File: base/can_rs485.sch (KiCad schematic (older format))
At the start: 15 parts, among them U21 SN65HVD230

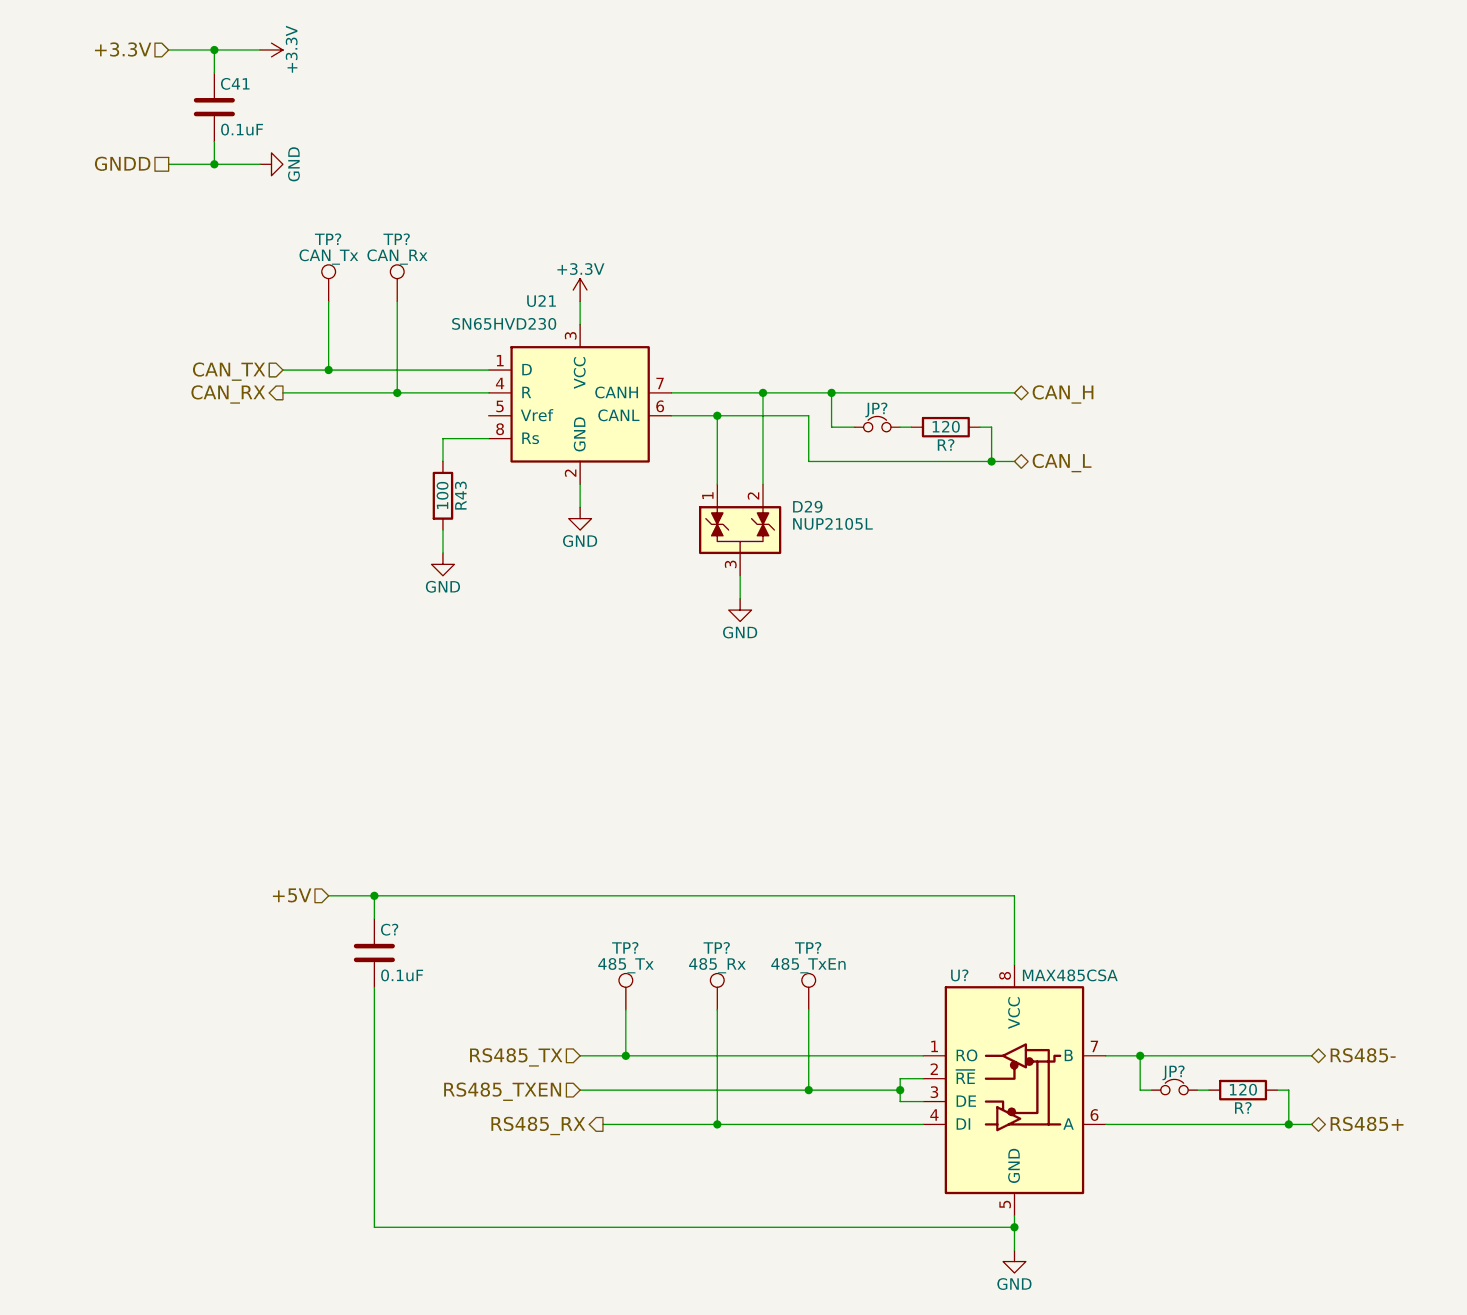
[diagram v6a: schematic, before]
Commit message: annotate sch
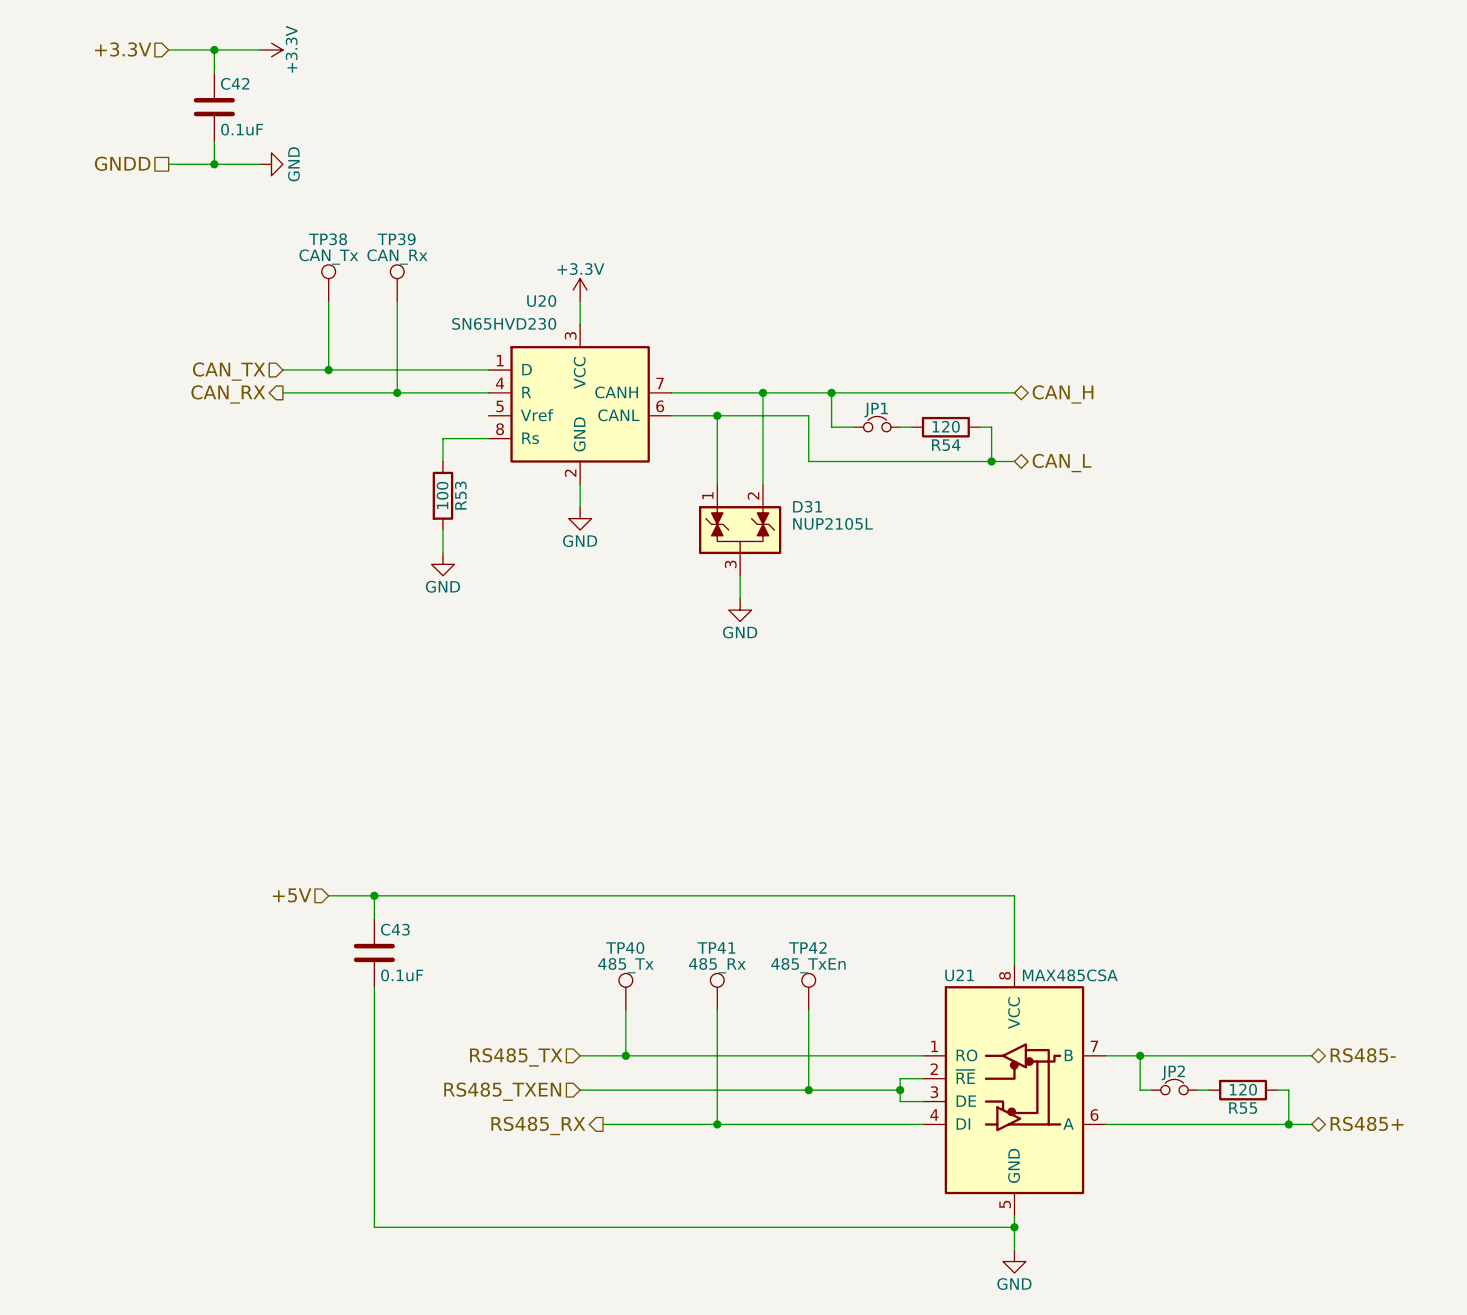
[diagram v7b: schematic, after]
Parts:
- gave numbers to parts that had none: 11
- renumbered C41 to C42, D29 to D31, R43 to R53, U21 to U20
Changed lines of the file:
@@
 +5V
 $Comp
-L SN65HVD230 U21
+L SN65HVD230 U20
 U 1 1 5A3C3395
 P 3100 2400
-F 0 "U21" H 3000 2800 50  0000 R CNN
+F 0 "U20" H 3000 2800 50  0000 R CNN
 F 1 "SN65HVD230" H 3000 2700 50  0000 R CNN
 F 2 "Package_SOIC:SOIC-8_3.9x4.9mm_P1.27mm" H 3100 1900 50  0001 C CNN
@@
 	3500 2400 5000 2400
 $Comp
-L C C41
+L C C42
 U 1 1 5A3C342C
 P 1500 1150
-F 0 "C41" H 1525 1250 50  0000 L CNN
+F 0 "C42" H 1525 1250 50  0000 L CNN
 F 1 "0.1uF" H 1525 1050 50  0000 L CNN
 F 2 "Capacitor_SMD:C_0603_1608Metric" H 1538 1000 50  0001 C CNN
@@
 GNDD
 $Comp
-L +3.3V #PWR027
+L +3.3V #PWR33
 U 1 1 5A3C351C
 P 1700 900
-F 0 "#PWR027" H 1700 750 50  0001 C CNN
+F 0 "#PWR33" H 1700 750 50  0001 C CNN
 F 1 "+3.3V" H 1700 1040 50  0000 C CNN
 F 2 "" H 1700 900 50  0001 C CNN
@@
 $EndComp
 $Comp
-L GND #PWR028
+L GND #PWR34
 U 1 1 5A3C3534
 P 1700 1400
-F 0 "#PWR028" H 1700 1150 50  0001 C CNN
+F 0 "#PWR34" H 1700 1150 50  0001 C CNN
 F 1 "GND" H 1700 1250 50  0000 C CNN
 F 2 "" H 1700 1400 50  0001 C CNN
@@
 $EndComp
 $Comp
-L GND #PWR029
+L GND #PWR37
 U 1 1 5A3C354C
 P 3100 2900
-F 0 "#PWR029" H 3100 2650 50  0001 C CNN
+F 0 "#PWR37" H 3100 2650 50  0001 C CNN
 F 1 "GND" H 3100 2750 50  0000 C CNN
 F 2 "" H 3100 2900 50  0001 C CNN
@@
 	3100 2900 3100 2800
 $Comp
-L +3.3V #PWR030
+L +3.3V #PWR36
 U 1 1 5A3C3569
 P 3100 2000
-F 0 "#PWR030" H 3100 1850 50  0001 C CNN
+F 0 "#PWR36" H 3100 1850 50  0001 C CNN
 F 1 "+3.3V" H 3100 2140 50  0000 C CNN
 F 2 "" H 3100 2000 50  0001 C CNN
@@
 	3100 2100 3100 2000
 $Comp
-L R R43
+L R R53
 U 1 1 5A3C3843
 P 2500 2850
-F 0 "R43" V 2580 2850 50  0000 C CNN
+F 0 "R53" V 2580 2850 50  0000 C CNN
 F 1 "100" V 2500 2850 50  0000 C CNN
 F 2 "Resistor_SMD:R_0603_1608Metric" V 2430 2850 50  0001 C CNN
@@
 	2500 3000 2500 3100
 $Comp
-L GND #PWR031
+L GND #PWR35
 U 1 1 5A3C38B7
 P 2500 3100
-F 0 "#PWR031" H 2500 2850 50  0001 C CNN
+F 0 "#PWR35" H 2500 2850 50  0001 C CNN
 F 1 "GND" H 2500 2950 50  0000 C CNN
 F 2 "" H 2500 3100 50  0001 C CNN
@@
 	1800 2400 2700 2400
 $Comp
-L NUP2105L D29
+L NUP2105L D31
 U 1 1 5A3C4E77
 P 3800 3000
-F 0 "D29" H 4025 3100 50  0000 L CNN
+F 0 "D31" H 4025 3100 50  0000 L CNN
 F 1 "NUP2105L" H 4025 3025 50  0000 L CNN
 F 2 "Package_TO_SOT_SMD:SOT-23" H 4025 2950 50  0001 L CNN
@@
 	3800 3200 3800 3300
 $Comp
-L GND #PWR032
+L GND #PWR38
 U 1 1 5A3C4FCE
 P 3800 3300
-F 0 "#PWR032" H 3800 3050 50  0001 C CNN
+F 0 "#PWR38" H 3800 3050 50  0001 C CNN
 F 1 "GND" H 3800 3150 50  0000 C CNN
 F 2 "" H 3800 3300 50  0001 C CNN
@@
 $EndComp
 $Comp
-L MAX485E U?
+L MAX485E U21
 U 1 1 5A44C7B1
 P 5000 5400
-F 0 "U?" H 4760 5850 50  0000 C CNN
+F 0 "U21" H 4760 5850 50  0000 C CNN
 F 1 "MAX485CSA" H 5030 5850 50  0000 L CNN
 F 2 "Package_SOIC:SO-8_5.3x6.2mm_P1.27mm" H 5000 4700 50  0001 C CNN
@@
 	5000 4600 5000 4900
 $Comp
-L GND #PWR033
+L GND #PWR39
 U 1 1 5A44CCE9
 P 5000 6150
-F 0 "#PWR033" H 5000 5900 50  0001 C CNN
+F 0 "#PWR39" H 5000 5900 50  0001 C CNN
 F 1 "GND" H 5000 6000 50  0000 C CNN
 F 2 "" H 5000 6150 50  0001 C CNN
@@
 	5000 6000 5000 6150
 $Comp
-L C C?
+L C C43
 U 1 1 5A44D127
 P 2200 4850
-F 0 "C?" H 2225 4950 50  0000 L CNN
+F 0 "C43" H 2225 4950 50  0000 L CNN
 F 1 "0.1uF" H 2225 4750 50  0000 L CNN
 F 2 "Capacitor_SMD:C_0603_1608Metric" H 2238 4700 50  0001 C CNN
@@
 	2200 6050 2200 5000
 $Comp
-L Jumper_NC_Small JP?
+L Jumper_NC_Small JP2
 U 1 1 5A44DA0F
 P 5700 5450
-F 0 "JP?" H 5700 5530 50  0000 C CNN
+F 0 "JP2" H 5700 5530 50  0000 C CNN
 F 1 "Jumper_NC_Small" H 5710 5390 50  0001 C CNN
 F 2 "Connector_PinHeader_2.54mm:PinHeader_1x02_P2.54mm_Vertical" H 5700 5450 50  0001 C CNN
@@
 $EndComp
 $Comp
-L R R?
+L R R55
 U 1 1 5A44DAB5
 P 6000 5450
-F 0 "R?" V 6080 5450 50  0000 C CNN
+F 0 "R55" V 6080 5450 50  0000 C CNN
 F 1 "120" V 6000 5450 50  0000 C CNN
 F 2 "Resistor_SMD:R_0603_1608Metric" V 5930 5450 50  0001 C CNN
@@
 Connection ~ 5550 5300
 $Comp
-L Jumper_NC_Small JP?
+L Jumper_NC_Small JP1
 U 1 1 5A450646
 P 4400 2550
-F 0 "JP?" H 4400 2630 50  0000 C CNN
+F 0 "JP1" H 4400 2630 50  0000 C CNN
 F 1 "Jumper_NC_Small" H 4410 2490 50  0001 C CNN
 F 2 "Connector_PinHeader_2.54mm:PinHeader_1x02_P2.54mm_Vertical" H 4400 2550 50  0001 C CNN
@@
 $EndComp
 $Comp
-L R R?
+L R R54
 U 1 1 5A45064C
 P 4700 2550
-F 0 "R?" V 4780 2550 50  0000 C CNN
+F 0 "R54" V 4780 2550 50  0000 C CNN
 F 1 "120" V 4700 2550 50  0000 C CNN
 F 2 "Resistor_SMD:R_0603_1608Metric" V 4630 2550 50  0001 C CNN
@@
 Connection ~ 2000 2300
 $Comp
-L Test_Point TP?
+L Test_Point TP38
 U 1 1 5A4582A3
 P 2000 2000
-F 0 "TP?" H 2000 2270 50  0000 C CNN
+F 0 "TP38" H 2000 2270 50  0000 C CNN
 F 1 "CAN_Tx" H 2000 2200 50  0000 C CNN
 F 2 "" H 2200 2000 50  0001 C CNN
@@
 $EndComp
 $Comp
-L Test_Point TP?
+L Test_Point TP39
 U 1 1 5A4582FF
 P 2300 2000
-F 0 "TP?" H 2300 2270 50  0000 C CNN
+F 0 "TP39" H 2300 2270 50  0000 C CNN
 F 1 "CAN_Rx" H 2300 2200 50  0000 C CNN
 F 2 "" H 2500 2000 50  0001 C CNN
@@
 Connection ~ 2300 2400
 $Comp
-L Test_Point TP?
+L Test_Point TP40
 U 1 1 5A458C5A
 P 3300 5100
-F 0 "TP?" H 3300 5370 50  0000 C CNN
+F 0 "TP40" H 3300 5370 50  0000 C CNN
 F 1 "485_Tx" H 3300 5300 50  0000 C CNN
 F 2 "" H 3500 5100 50  0001 C CNN
@@
 $EndComp
 $Comp
-L Test_Point TP?
+L Test_Point TP41
 U 1 1 5A458D89
 P 3700 5100
-F 0 "TP?" H 3700 5370 50  0000 C CNN
+F 0 "TP41" H 3700 5370 50  0000 C CNN
 F 1 "485_Rx" H 3700 5300 50  0000 C CNN
 F 2 "" H 3900 5100 50  0001 C CNN
@@
 $EndComp
 $Comp
-L Test_Point TP?
+L Test_Point TP42
 U 1 1 5A458E0D
 P 4100 5100
-F 0 "TP?" H 4100 5370 50  0000 C CNN
+F 0 "TP42" H 4100 5370 50  0000 C CNN
 F 1 "485_TxEn" H 4100 5300 50  0000 C CNN
 F 2 "" H 4300 5100 50  0001 C CNN

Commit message: added footprints, created netlist
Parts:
- TP38, TP39, TP40, TP41, TP42: footprint (none) -> TestPoint:TestPoint_Pad_D1.5mm
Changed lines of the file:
@@
 GNDD
 $Comp
-L +3.3V #PWR33
+L +3.3V #PWR033
 U 1 1 5A3C351C
 P 1700 900
-F 0 "#PWR33" H 1700 750 50  0001 C CNN
+F 0 "#PWR033" H 1700 750 50  0001 C CNN
 F 1 "+3.3V" H 1700 1040 50  0000 C CNN
 F 2 "" H 1700 900 50  0001 C CNN
@@
 $EndComp
 $Comp
-L GND #PWR34
+L GND #PWR034
 U 1 1 5A3C3534
 P 1700 1400
-F 0 "#PWR34" H 1700 1150 50  0001 C CNN
+F 0 "#PWR034" H 1700 1150 50  0001 C CNN
 F 1 "GND" H 1700 1250 50  0000 C CNN
 F 2 "" H 1700 1400 50  0001 C CNN
@@
 $EndComp
 $Comp
-L GND #PWR37
+L GND #PWR035
 U 1 1 5A3C354C
 P 3100 2900
-F 0 "#PWR37" H 3100 2650 50  0001 C CNN
+F 0 "#PWR035" H 3100 2650 50  0001 C CNN
 F 1 "GND" H 3100 2750 50  0000 C CNN
 F 2 "" H 3100 2900 50  0001 C CNN
@@
 	3100 2900 3100 2800
 $Comp
-L +3.3V #PWR36
+L +3.3V #PWR036
 U 1 1 5A3C3569
 P 3100 2000
-F 0 "#PWR36" H 3100 1850 50  0001 C CNN
+F 0 "#PWR036" H 3100 1850 50  0001 C CNN
 F 1 "+3.3V" H 3100 2140 50  0000 C CNN
 F 2 "" H 3100 2000 50  0001 C CNN
@@
 	2500 3000 2500 3100
 $Comp
-L GND #PWR35
+L GND #PWR037
 U 1 1 5A3C38B7
 P 2500 3100
-F 0 "#PWR35" H 2500 2850 50  0001 C CNN
+F 0 "#PWR037" H 2500 2850 50  0001 C CNN
 F 1 "GND" H 2500 2950 50  0000 C CNN
 F 2 "" H 2500 3100 50  0001 C CNN
@@
 	3800 3200 3800 3300
 $Comp
-L GND #PWR38
+L GND #PWR038
 U 1 1 5A3C4FCE
 P 3800 3300
-F 0 "#PWR38" H 3800 3050 50  0001 C CNN
+F 0 "#PWR038" H 3800 3050 50  0001 C CNN
 F 1 "GND" H 3800 3150 50  0000 C CNN
 F 2 "" H 3800 3300 50  0001 C CNN
@@
 	5000 4600 5000 4900
 $Comp
-L GND #PWR39
+L GND #PWR039
 U 1 1 5A44CCE9
 P 5000 6150
-F 0 "#PWR39" H 5000 5900 50  0001 C CNN
+F 0 "#PWR039" H 5000 5900 50  0001 C CNN
 F 1 "GND" H 5000 6000 50  0000 C CNN
 F 2 "" H 5000 6150 50  0001 C CNN
@@
 F 0 "TP38" H 2000 2270 50  0000 C CNN
 F 1 "CAN_Tx" H 2000 2200 50  0000 C CNN
-F 2 "" H 2200 2000 50  0001 C CNN
+F 2 "TestPoint:TestPoint_Pad_D1.5mm" H 2200 2000 50  0001 C CNN
 F 3 "" H 2200 2000 50  0001 C CNN
 	1    2000 2000
@@
 F 0 "TP39" H 2300 2270 50  0000 C CNN
 F 1 "CAN_Rx" H 2300 2200 50  0000 C CNN
-F 2 "" H 2500 2000 50  0001 C CNN
+F 2 "TestPoint:TestPoint_Pad_D1.5mm" H 2500 2000 50  0001 C CNN
 F 3 "" H 2500 2000 50  0001 C CNN
 	1    2300 2000
@@
 F 0 "TP40" H 3300 5370 50  0000 C CNN
 F 1 "485_Tx" H 3300 5300 50  0000 C CNN
-F 2 "" H 3500 5100 50  0001 C CNN
+F 2 "TestPoint:TestPoint_Pad_D1.5mm" H 3500 5100 50  0001 C CNN
 F 3 "" H 3500 5100 50  0001 C CNN
 	1    3300 5100
@@
 F 0 "TP41" H 3700 5370 50  0000 C CNN
 F 1 "485_Rx" H 3700 5300 50  0000 C CNN
-F 2 "" H 3900 5100 50  0001 C CNN
+F 2 "TestPoint:TestPoint_Pad_D1.5mm" H 3900 5100 50  0001 C CNN
 F 3 "" H 3900 5100 50  0001 C CNN
 	1    3700 5100
@@
 F 0 "TP42" H 4100 5370 50  0000 C CNN
 F 1 "485_TxEn" H 4100 5300 50  0000 C CNN
-F 2 "" H 4300 5100 50  0001 C CNN
+F 2 "TestPoint:TestPoint_Pad_D1.5mm" H 4300 5100 50  0001 C CNN
 F 3 "" H 4300 5100 50  0001 C CNN
 	1    4100 5100
